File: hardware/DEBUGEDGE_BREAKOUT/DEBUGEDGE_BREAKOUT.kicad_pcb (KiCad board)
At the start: 2 copper layers, 17.8 x 27.9 mm, 4 parts, among them J1 DebugEdge_02x05, J2 Conn_ARM_JTAG_SWD_10, J3 Conn_01x10_Pin

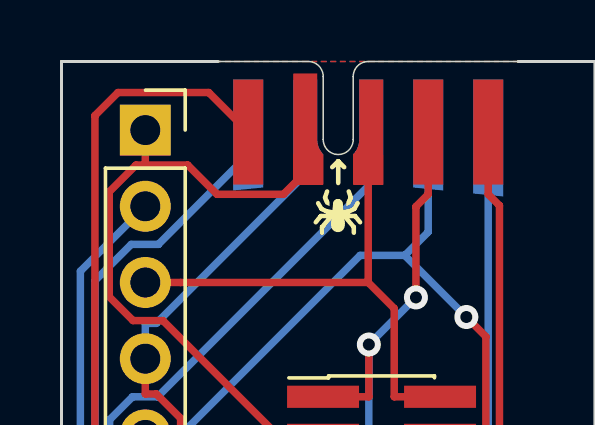
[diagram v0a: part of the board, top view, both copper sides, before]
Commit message: Fix footprints and jlc placeholder in DebugEdge Breakout
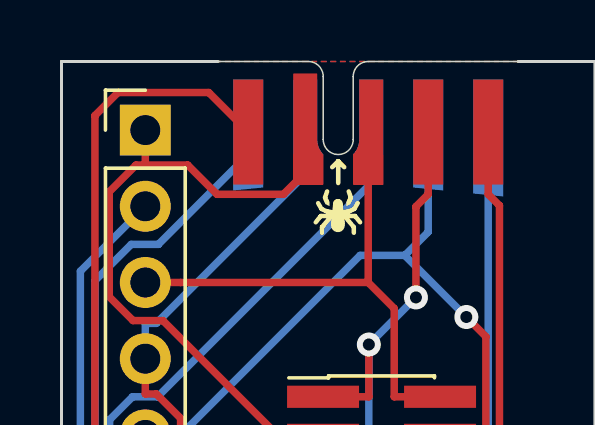
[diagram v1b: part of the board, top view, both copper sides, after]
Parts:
- J3: footprint Connector_PinSocket_2.54mm:PinSocket_1x10_P2.54mm_Vertical -> Connector_PinHeader_2.54mm:PinHeader_1x10_P2.54mm_Vertical
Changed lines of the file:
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@@
   (net 10 "TRACE1")
   (net 11 "unconnected-(J2-KEY-Pad7)")
-  (footprint "Connector_PinSocket_2.54mm:PinSocket_1x10_P2.54mm_Vertical" (layer "F.Cu")
+  (footprint "Connector_PinHeader_2.54mm:PinHeader_1x10_P2.54mm_Vertical" (layer "F.Cu")
     (at 119.634 73.406)
-    (descr "Through hole straight socket strip, 1x10, 2.54mm pitch, single row (from Kicad 4.0.7), script generated")
-    (tags "Through hole socket strip THT 1x10 2.54mm single row")
+    (descr "Through hole straight pin header, 1x10, 2.54mm pitch, single row")
+    (tags "Through hole pin header THT 1x10 2.54mm single row")
     (property "Sheetfile" "DEBUGEDGE_BREAKOUT.kicad_sch")
     (property "Sheetname" "")
@@
     (property "ki_keywords" "connector")
     (attr through_hole)
-    (fp_text reference "J3" (at 0 -2.77) (layer "F.SilkS") hide
+    (fp_text reference "J3" (at 0 -2.33) (layer "F.SilkS") hide
         (effects (font (size 1 1) (thickness 0.15)))
     )
-    (fp_text value "Conn_01x10_Pin" (at 0 25.63) (layer "F.Fab") hide
+    (fp_text value "Conn_01x10_Pin" (at 0 25.19) (layer "F.Fab") hide
         (effects (font (size 1 1) (thickness 0.15)))
     )
@@
         (effects (font (size 1 1) (thickness 0.15)))
     )
+    (fp_line (start -1.33 -1.33) (end 0 -1.33)
+      (stroke (width 0.12) (type solid)) (layer "F.SilkS"))
+    (fp_line (start -1.33 0) (end -1.33 -1.33)
+      (stroke (width 0.12) (type solid)) (layer "F.SilkS"))
     (fp_line (start -1.33 1.27) (end -1.33 24.19)
       (stroke (width 0.12) (type solid)) (layer "F.SilkS"))
@@
     (fp_line (start -1.33 24.19) (end 1.33 24.19)
       (stroke (width 0.12) (type solid)) (layer "F.SilkS"))
-    (fp_line (start 0 -1.33) (end 1.33 -1.33)
-      (stroke (width 0.12) (type solid)) (layer "F.SilkS"))
-    (fp_line (start 1.33 -1.33) (end 1.33 0)
-      (stroke (width 0.12) (type solid)) (layer "F.SilkS"))
     (fp_line (start 1.33 1.27) (end 1.33 24.19)
       (stroke (width 0.12) (type solid)) (layer "F.SilkS"))
-    (fp_line (start -1.8 -1.8) (end 1.75 -1.8)
-      (stroke (width 0.05) (type solid)) (layer "F.CrtYd"))
-    (fp_line (start -1.8 24.6) (end -1.8 -1.8)
-      (stroke (width 0.05) (type solid)) (layer "F.CrtYd"))
-    (fp_line (start 1.75 -1.8) (end 1.75 24.6)
-      (stroke (width 0.05) (type solid)) (layer "F.CrtYd"))
-    (fp_line (start 1.75 24.6) (end -1.8 24.6)
-      (stroke (width 0.05) (type solid)) (layer "F.CrtYd"))
-    (fp_line (start -1.27 -1.27) (end 0.635 -1.27)
-      (stroke (width 0.1) (type solid)) (layer "F.Fab"))
-    (fp_line (start -1.27 24.13) (end -1.27 -1.27)
-      (stroke (width 0.1) (type solid)) (layer "F.Fab"))
-    (fp_line (start 0.635 -1.27) (end 1.27 -0.635)
-      (stroke (width 0.1) (type solid)) (layer "F.Fab"))
-    (fp_line (start 1.27 -0.635) (end 1.27 24.13)
+    (fp_line (start -1.8 -1.8) (end -1.8 24.65)
+      (stroke (width 0.05) (type solid)) (layer "F.CrtYd"))
+    (fp_line (start -1.8 24.65) (end 1.8 24.65)
+      (stroke (width 0.05) (type solid)) (layer "F.CrtYd"))
+    (fp_line (start 1.8 -1.8) (end -1.8 -1.8)
+      (stroke (width 0.05) (type solid)) (layer "F.CrtYd"))
+    (fp_line (start 1.8 24.65) (end 1.8 -1.8)
+      (stroke (width 0.05) (type solid)) (layer "F.CrtYd"))
+    (fp_line (start -1.27 -0.635) (end -0.635 -1.27)
+      (stroke (width 0.1) (type solid)) (layer "F.Fab"))
+    (fp_line (start -1.27 24.13) (end -1.27 -0.635)
+      (stroke (width 0.1) (type solid)) (layer "F.Fab"))
+    (fp_line (start -0.635 -1.27) (end 1.27 -1.27)
+      (stroke (width 0.1) (type solid)) (layer "F.Fab"))
+    (fp_line (start 1.27 -1.27) (end 1.27 24.13)
       (stroke (width 0.1) (type solid)) (layer "F.Fab"))
     (fp_line (start 1.27 24.13) (end -1.27 24.13)
@@
     (pad "10" thru_hole oval (at 0 22.86) (size 1.7 1.7) (drill 1) (layers "*.Cu" "*.Mask")
       (net 10 "TRACE1") (pinfunction "Pin_10") (pintype "passive"))
-    (model "${KICAD6_3DMODEL_DIR}/Connector_PinSocket_2.54mm.3dshapes/PinSocket_1x10_P2.54mm_Vertical.wrl"
+    (model "${KICAD6_3DMODEL_DIR}/Connector_PinHeader_2.54mm.3dshapes/PinHeader_1x10_P2.54mm_Vertical.wrl"
       (offset (xyz 0 0 0))
       (scale (xyz 1 1 1))
@@
   (gr_line (start 116.84 71.12) (end 122.064 71.12)
     (stroke (width 0.1) (type default)) (layer "Edge.Cuts"))
-  (gr_text "JLCJLCJLC" (at 130.048 97.79) (layer "B.SilkS")
-    (effects (font (size 1 1) (thickness 0.15)) (justify right bottom))
+  (gr_text "JLCJLCJLC" (at 126.492 97.79) (layer "B.SilkS")
+    (effects (font (size 1 1) (thickness 0.15)) (justify right bottom mirror))
   )
   (gr_text "DEBUGEDGE_SWD" (at 121.666 97.79) (layer "F.SilkS")
